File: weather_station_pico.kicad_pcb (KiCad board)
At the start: 2 copper layers, 88.5 x 90 mm, 30 parts, among them J1 POWER, J2 WSPEED, J3 WDIR, J4 I2C, SW1 SW_Push, U1 LM7805_TO220, U2 E220-900T22D, U3 Pico, U4 74HC4051, U5 LM35-LP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

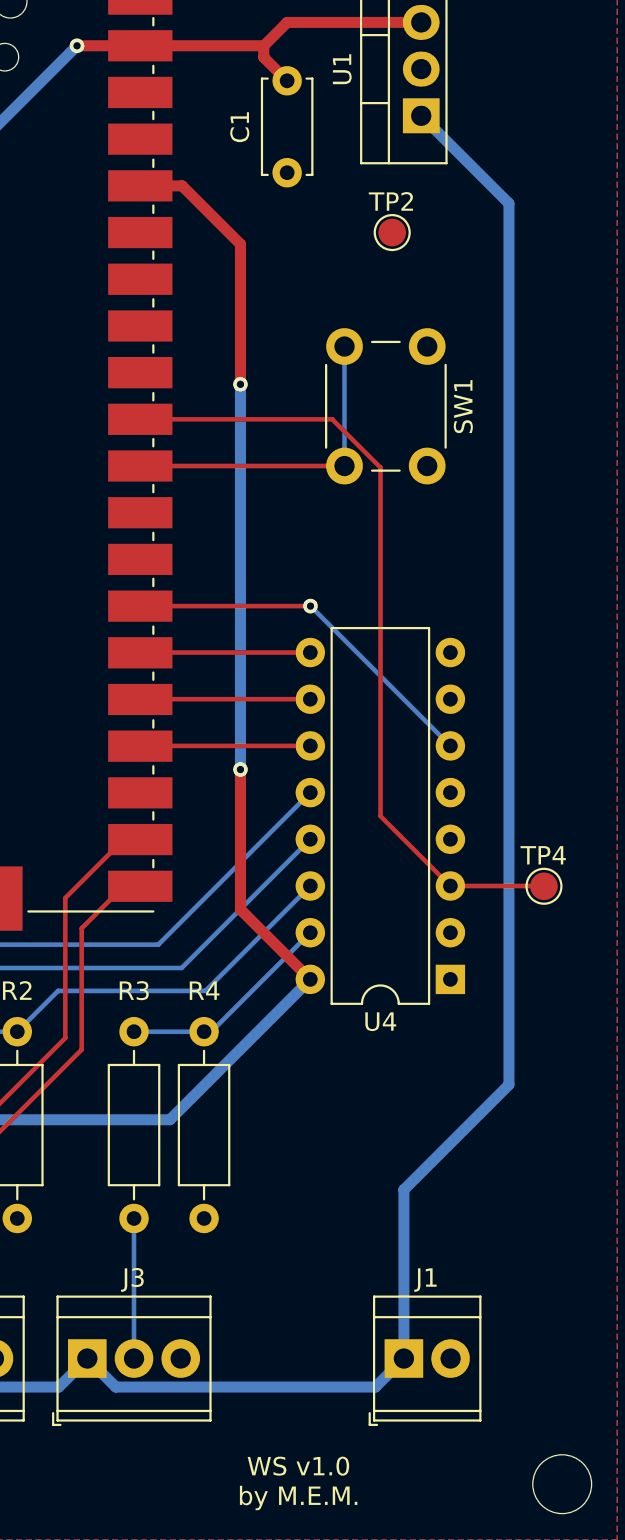
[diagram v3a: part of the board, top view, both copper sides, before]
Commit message: replace power connector
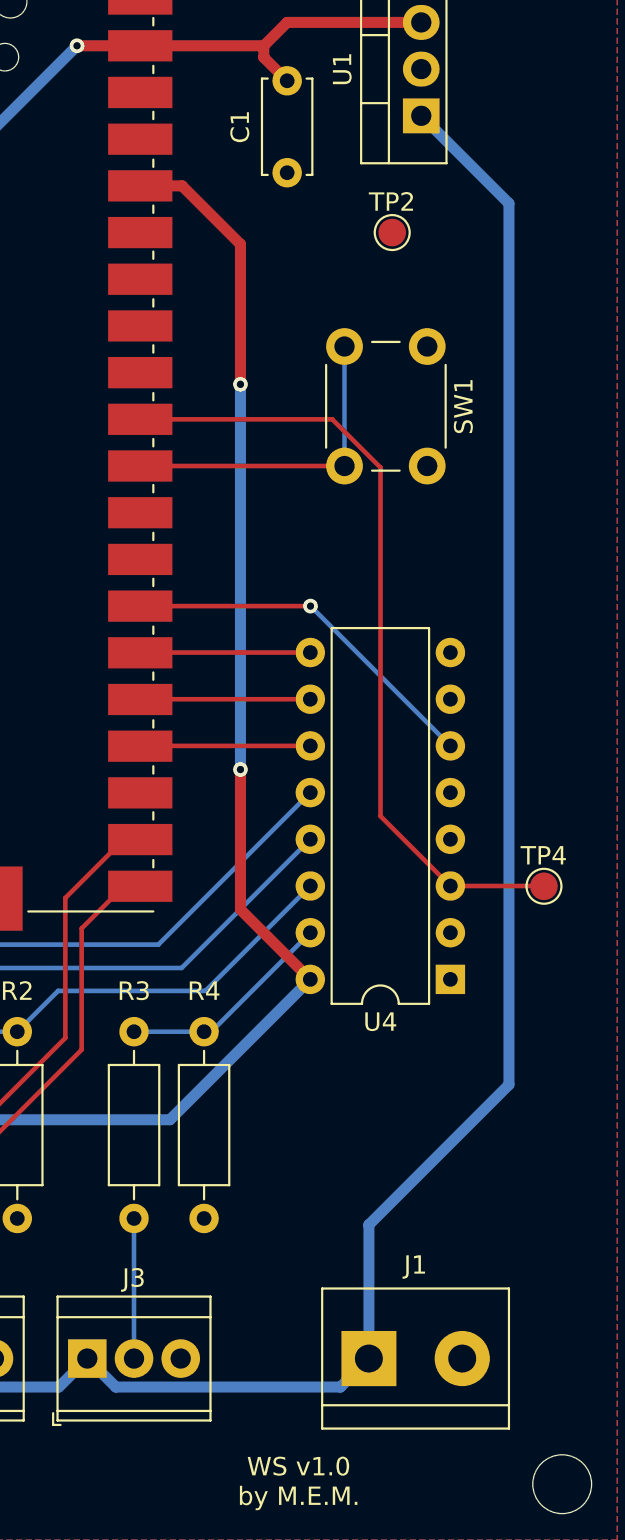
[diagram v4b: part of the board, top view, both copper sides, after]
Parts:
- J1: footprint TerminalBlock_TE-Connectivity:TerminalBlock_TE_282834-2_1x02_P2.54mm_Horizontal -> TerminalBlock:TerminalBlock_bornier-2_P5.08mm
- moved J1 1.91 mm to (182.2, 126.0)
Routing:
- net +12V: track 122.6 -> 121.5 mm
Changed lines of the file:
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@@
     )
   )
-  (footprint "TerminalBlock_TE-Connectivity:TerminalBlock_TE_282834-2_1x02_P2.54mm_Horizontal" (layer "F.Cu")
-    (at 184.15 126.02)
-    (descr "Terminal Block TE 282834-2, 2 pins, pitch 2.54mm, size 5.54x6.5mm^2, drill diamater 1.1mm, pad diameter 2.1mm, see http://www.te.com/commerce/DocumentDelivery/DDEController?Action=showdoc&DocId=Customer+Drawing%7F282834%7FC1%7Fpdf%7FEnglish%7FENG_CD_282834_C1.pdf, script-generated using https://github.com/pointhi/kicad-footprint-generator/scripts/TerminalBlock_TE-Connectivity")
-    (tags "THT Terminal Block TE 282834-2 pitch 2.54mm size 5.54x6.5mm^2 drill 1.1mm pad 2.1mm")
-    (property "Sheetfile" "weather_station_pico.kicad_sch")
-    (property "Sheetname" "")
-    (attr through_hole)
-    (fp_text reference "J1" (at 1.27 -4.37) (layer "F.SilkS")
-      (effects (font (size 1 1) (thickness 0.15)))
-    )
-    (fp_text value "POWER" (at 1.27 4.37) (layer "F.Fab")
-      (effects (font (size 1 1) (thickness 0.15)))
-    )
-    (fp_text user "${REFERENCE}" (at 1.27 2) (layer "F.Fab")
-      (effects (font (size 1 1) (thickness 0.15)))
-    )
-    (fp_line (start -1.62 -3.37) (end 4.16 -3.37) (layer "F.SilkS") (width 0.12))
-    (fp_line (start -1.86 3.61) (end -1.46 3.61) (layer "F.SilkS") (width 0.12))
-    (fp_line (start 4.16 -3.37) (end 4.16 3.37) (layer "F.SilkS") (width 0.12))
-    (fp_line (start -1.62 2.85) (end 4.16 2.85) (layer "F.SilkS") (width 0.12))
-    (fp_line (start -1.62 3.37) (end 4.16 3.37) (layer "F.SilkS") (width 0.12))
-    (fp_line (start -1.62 -3.37) (end -1.62 3.37) (layer "F.SilkS") (width 0.12))
-    (fp_line (start -1.86 2.97) (end -1.86 3.61) (layer "F.SilkS") (width 0.12))
-    (fp_line (start -1.62 -2.25) (end 4.16 -2.25) (layer "F.SilkS") (width 0.12))
-    (fp_line (start 4.54 3.75) (end 4.54 -3.75) (layer "F.CrtYd") (width 0.05))
-    (fp_line (start -2 3.75) (end 4.54 3.75) (layer "F.CrtYd") (width 0.05))
-    (fp_line (start -2 -3.75) (end -2 3.75) (layer "F.CrtYd") (width 0.05))
-    (fp_line (start 4.54 -3.75) (end -2 -3.75) (layer "F.CrtYd") (width 0.05))
-    (fp_line (start -1.5 -2.25) (end 4.04 -2.25) (layer "F.Fab") (width 0.1))
-    (fp_line (start 4.04 -3.25) (end 4.04 3.25) (layer "F.Fab") (width 0.1))
-    (fp_line (start 3.241 -0.835) (end 1.706 0.7) (layer "F.Fab") (width 0.1))
-    (fp_line (start -1.5 -3.25) (end 4.04 -3.25) (layer "F.Fab") (width 0.1))
-    (fp_line (start 0.701 -0.835) (end -0.835 0.7) (layer "F.Fab") (width 0.1))
-    (fp_line (start -1.1 3.25) (end -1.5 2.85) (layer "F.Fab") (width 0.1))
-    (fp_line (start -1.5 2.85) (end 4.04 2.85) (layer "F.Fab") (width 0.1))
-    (fp_line (start 3.375 -0.7) (end 1.84 0.835) (layer "F.Fab") (width 0.1))
-    (fp_line (start -1.5 2.85) (end -1.5 -3.25) (layer "F.Fab") (width 0.1))
-    (fp_line (start 4.04 3.25) (end -1.1 3.25) (layer "F.Fab") (width 0.1))
-    (fp_line (start 0.835 -0.7) (end -0.701 0.835) (layer "F.Fab") (width 0.1))
-    (fp_circle (center 2.54 0) (end 3.64 0) (layer "F.Fab") (width 0.1) (fill none))
-    (fp_circle (center 0 0) (end 1.1 0) (layer "F.Fab") (width 0.1) (fill none))
-    (pad "1" thru_hole rect (at 0 0) (size 2.1 2.1) (drill 1.1) (layers *.Cu *.Mask)
+  (footprint "TerminalBlock:TerminalBlock_bornier-2_P5.08mm" (layer "F.Cu")
+    (at 182.245 126.02)
+    (descr "simple 2-pin terminal block, pitch 5.08mm, revamped version of bornier2")
+    (tags "terminal block bornier2")
+    (property "Sheetfile" "weather_station_pico.kicad_sch")
+    (property "Sheetname" "")
+    (attr through_hole)
+    (fp_text reference "J1" (at 2.54 -5.08) (layer "F.SilkS")
+      (effects (font (size 1 1) (thickness 0.15)))
+    )
+    (fp_text value "POWER" (at 2.54 5.08) (layer "F.Fab")
+      (effects (font (size 1 1) (thickness 0.15)))
+    )
+    (fp_text user "${REFERENCE}" (at 2.54 0) (layer "F.Fab")
+      (effects (font (size 1 1) (thickness 0.15)))
+    )
+    (fp_line (start -2.54 3.81) (end 7.62 3.81) (layer "F.SilkS") (width 0.12))
+    (fp_line (start 7.62 3.81) (end 7.62 -3.81) (layer "F.SilkS") (width 0.12))
+    (fp_line (start 7.62 -3.81) (end -2.54 -3.81) (layer "F.SilkS") (width 0.12))
+    (fp_line (start 7.62 2.54) (end -2.54 2.54) (layer "F.SilkS") (width 0.12))
+    (fp_line (start -2.54 -3.81) (end -2.54 3.81) (layer "F.SilkS") (width 0.12))
+    (fp_line (start -2.71 -4) (end 7.79 -4) (layer "F.CrtYd") (width 0.05))
+    (fp_line (start 7.79 4) (end -2.71 4) (layer "F.CrtYd") (width 0.05))
+    (fp_line (start -2.71 -4) (end -2.71 4) (layer "F.CrtYd") (width 0.05))
+    (fp_line (start 7.79 4) (end 7.79 -4) (layer "F.CrtYd") (width 0.05))
+    (fp_line (start -2.46 -3.75) (end -2.46 3.75) (layer "F.Fab") (width 0.1))
+    (fp_line (start 7.54 -3.75) (end -2.46 -3.75) (layer "F.Fab") (width 0.1))
+    (fp_line (start -2.46 3.75) (end 7.54 3.75) (layer "F.Fab") (width 0.1))
+    (fp_line (start -2.41 2.55) (end 7.49 2.55) (layer "F.Fab") (width 0.1))
+    (fp_line (start 7.54 3.75) (end 7.54 -3.75) (layer "F.Fab") (width 0.1))
+    (pad "1" thru_hole rect (at 0 0) (size 3 3) (drill 1.52) (layers *.Cu *.Mask)
       (net 1 "+12V") (pinfunction "Pin_1") (pintype "passive"))
-    (pad "2" thru_hole circle (at 2.54 0) (size 2.1 2.1) (drill 1.1) (layers *.Cu *.Mask)
+    (pad "2" thru_hole circle (at 5.08 0) (size 3 3) (drill 1.52) (layers *.Cu *.Mask)
       (net 2 "GND") (pinfunction "Pin_2") (pintype "passive"))
-    (model "${KICAD6_3DMODEL_DIR}/TerminalBlock_TE-Connectivity.3dshapes/TerminalBlock_TE_282834-2_1x02_P2.54mm_Horizontal.wrl"
-      (offset (xyz 0 0 0))
+    (model "${KICAD6_3DMODEL_DIR}/TerminalBlock.3dshapes/TerminalBlock_bornier-2_P5.08mm.wrl"
+      (offset (xyz 2.539999962 0 0))
       (scale (xyz 1 1 1))
       (rotate (xyz 0 0 0))
@@
     (effects (font (size 1 1) (thickness 0.15)))
   )
-  (segment (start 189.865 111.125) (end 189.865 63.19) (width 0.6) (layer "B.Cu") (net 1))
   (segment (start 158.319511 127.569511) (end 156.77 126.02) (width 0.6) (layer "B.Cu") (net 1))
+  (segment (start 168.479511 127.569511) (end 180.695489 127.569511) (width 0.6) (layer "B.Cu") (net 1))
+  (segment (start 180.695489 127.569511) (end 182.245 126.02) (width 0.6) (layer "B.Cu") (net 1))
   (segment (start 165.380489 127.569511) (end 158.319511 127.569511) (width 0.6) (layer "B.Cu") (net 1))
-  (segment (start 184.15 116.84) (end 189.865 111.125) (width 0.6) (layer "B.Cu") (net 1))
+  (segment (start 185.095 58.42) (end 189.865 63.19) (width 0.6) (layer "B.Cu") (net 1))
+  (segment (start 189.865 63.19) (end 189.865 111.125) (width 0.6) (layer "B.Cu") (net 1))
   (segment (start 140.96 114.115) (end 152.865 126.02) (width 0.6) (layer "B.Cu") (net 1))
-  (segment (start 189.865 63.19) (end 185.095 58.42) (width 0.6) (layer "B.Cu") (net 1))
   (segment (start 168.479511 127.569511) (end 166.93 126.02) (width 0.6) (layer "B.Cu") (net 1))
   (segment (start 166.93 126.02) (end 165.380489 127.569511) (width 0.6) (layer "B.Cu") (net 1))
-  (segment (start 182.600489 127.569511) (end 168.479511 127.569511) (width 0.6) (layer "B.Cu") (net 1))
-  (segment (start 184.15 126.02) (end 184.15 116.84) (width 0.6) (layer "B.Cu") (net 1))
+  (segment (start 189.865 111.125) (end 182.245 118.745) (width 0.6) (layer "B.Cu") (net 1))
+  (segment (start 182.245 118.745) (end 182.245 126.02) (width 0.6) (layer "B.Cu") (net 1))
   (segment (start 152.865 126.02) (end 156.77 126.02) (width 0.6) (layer "B.Cu") (net 1))
-  (segment (start 184.15 126.02) (end 182.600489 127.569511) (width 0.6) (layer "B.Cu") (net 1))
   (segment (start 159.31 118.4) (end 159.31 126.02) (width 0.25) (layer "B.Cu") (net 3))
   (segment (start 169.47 118.4) (end 169.47 126.02) (width 0.25) (layer "B.Cu") (net 4))

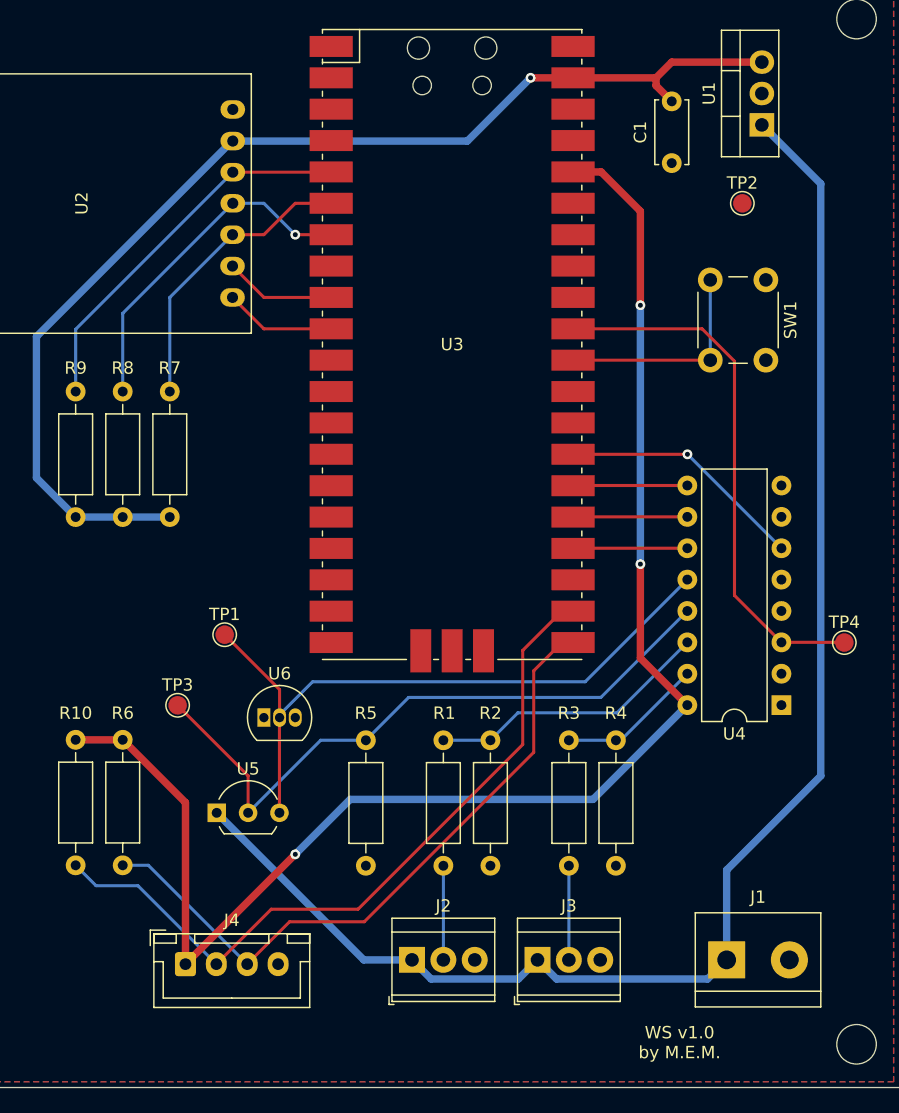
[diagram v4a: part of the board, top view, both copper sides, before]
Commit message: add terminal, remove jst connector
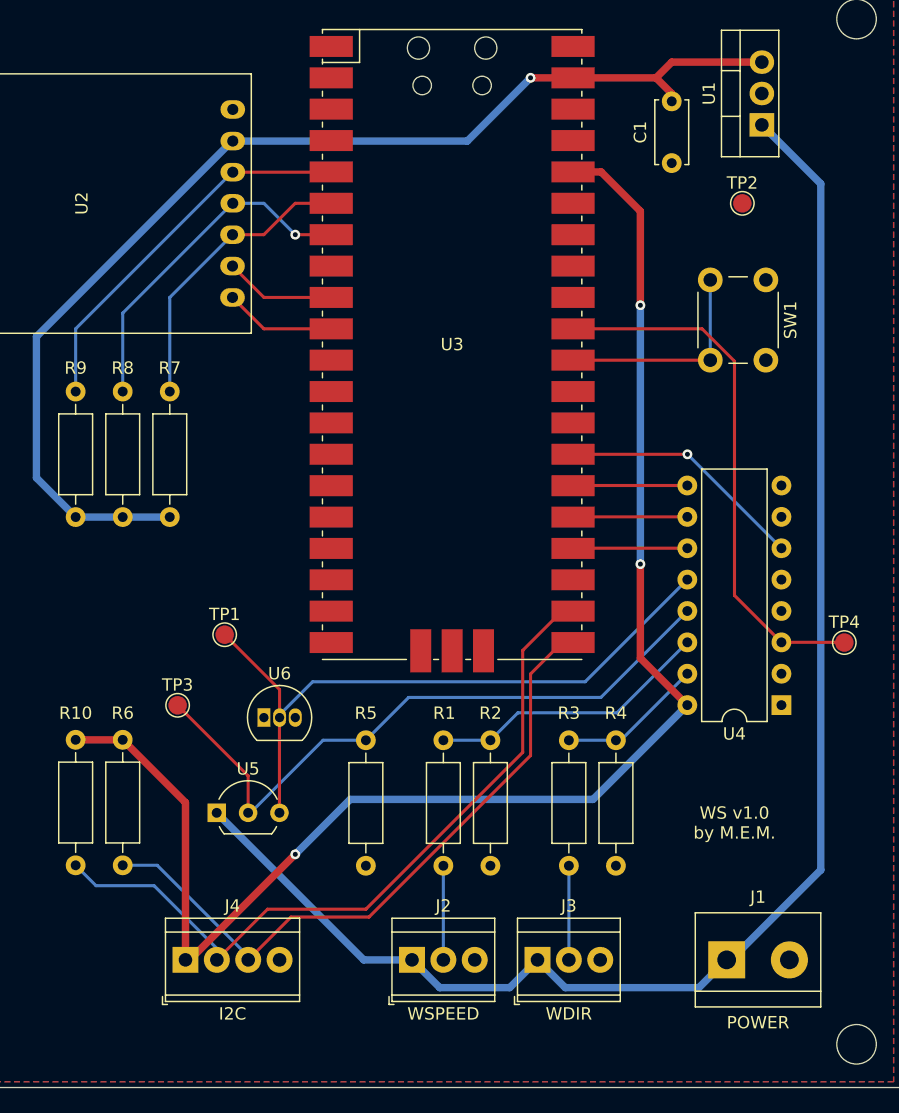
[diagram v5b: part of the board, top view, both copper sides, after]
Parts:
- J4: footprint Connector_JST:JST_XH_B4B-XH-A_1x04_P2.50mm_Vertical -> TerminalBlock_TE-Connectivity:TerminalBlock_TE_282834-4_1x04_P2.54mm_Horizontal
- moved J4 0.34 mm to (138.4, 126.0)
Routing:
- net +12V: track 121.5 -> 122.9 mm
- net /SCL: track 59.0 -> 59.6 mm

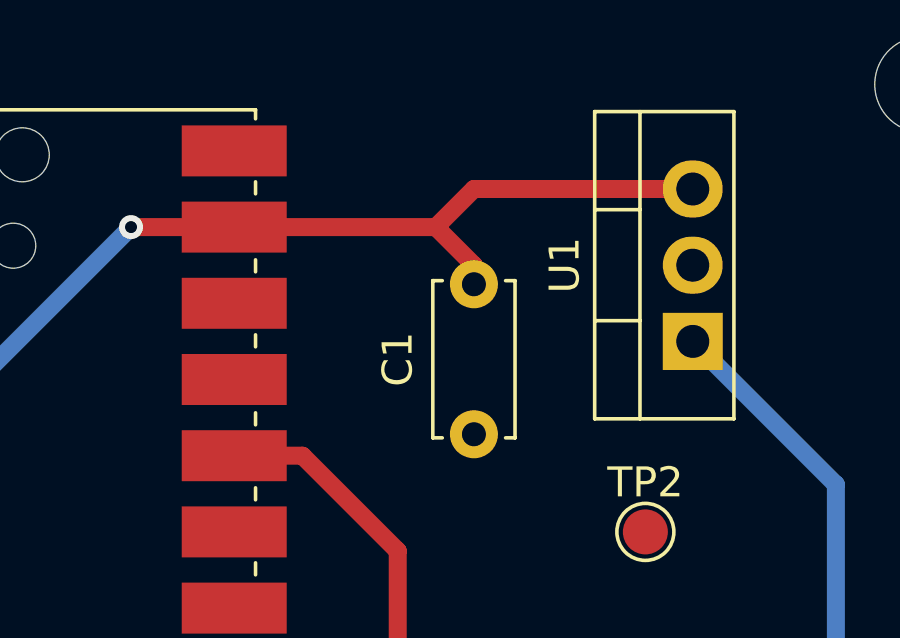
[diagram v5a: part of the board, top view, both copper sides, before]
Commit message: move capacitor, more simple track
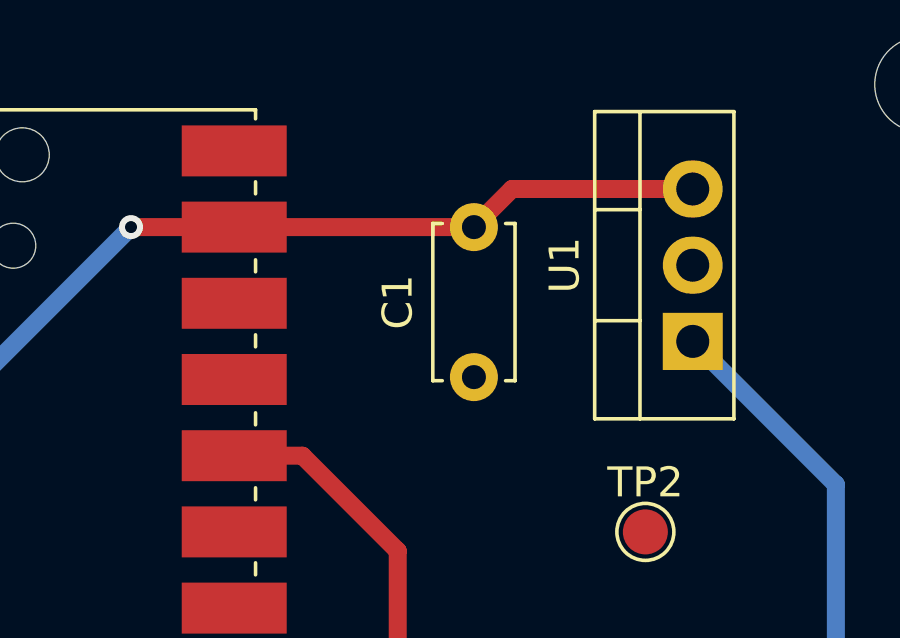
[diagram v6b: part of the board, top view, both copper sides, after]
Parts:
- C1: value C -> 0.1uF
- moved C1 1.91 mm to (177.8, 54.6)
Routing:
- net +5V: track 93.9 -> 91.5 mm
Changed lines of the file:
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@@
   )
   (footprint "Capacitor_THT:C_Disc_D5.0mm_W2.5mm_P5.00mm" (layer "F.Cu")
-    (at 177.8 56.515 -90)
+    (at 177.8 54.61 -90)
     (descr "C, Disc series, Radial, pin pitch=5.00mm, , diameter*width=5*2.5mm^2, Capacitor, http://cdn-reichelt.de/documents/datenblatt/B300/DS_KERKO_TC.pdf")
     (tags "C Disc series Radial pin pitch 5.00mm  diameter 5mm width 2.5mm Capacitor")
@@
       (effects (font (size 1 1) (thickness 0.15)))
     )
-    (fp_text value "C" (at 2.5 -2.54 90) (layer "F.Fab")
+    (fp_text value "0.1uF" (at 5.08 -2.54 90) (layer "F.Fab")
       (effects (font (size 1 1) (thickness 0.15)))
     )
@@
   (segment (start 159.31 118.4) (end 159.31 126.02) (width 0.25) (layer "B.Cu") (net 3))
   (segment (start 169.47 118.4) (end 169.47 126.02) (width 0.25) (layer "B.Cu") (net 4))
-  (segment (start 177.8 55.88) (end 177.8 56.515) (width 0.6) (layer "F.Cu") (net 6))
-  (segment (start 176.53 54.61) (end 177.8 55.88) (width 0.6) (layer "F.Cu") (net 6))
-  (segment (start 176.53 54.61) (end 168.91 54.61) (width 0.6) (layer "F.Cu") (net 6))
-  (segment (start 177.8 53.34) (end 176.53 54.61) (width 0.6) (layer "F.Cu") (net 6))
-  (segment (start 185.095 53.34) (end 177.8 53.34) (width 0.6) (layer "F.Cu") (net 6))
+  (segment (start 179.07 53.34) (end 177.8 54.61) (width 0.6) (layer "F.Cu") (net 6))
+  (segment (start 185.095 53.34) (end 179.07 53.34) (width 0.6) (layer "F.Cu") (net 6))
+  (segment (start 177.8 54.61) (end 168.91 54.61) (width 0.6) (layer "F.Cu") (net 6))
   (segment (start 166.37 54.61) (end 168.91 54.61) (width 0.6) (layer "F.Cu") (net 6))
   (via (at 166.37 54.61) (size 0.8) (drill 0.4) (layers "F.Cu" "B.Cu") (net 6))
